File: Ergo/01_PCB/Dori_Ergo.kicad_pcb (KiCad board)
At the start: 2 copper layers, 306.4 x 117.5 mm, 207 parts, among them J1 TYPE-C-31-M12_13, J2 AVR-ISP-6_mod, J3 4PIN, J4 4PIN, J5 TYPE-C-31-M12_13, J6 AVR-ISP-6_mod, K1 KEYSW, K10 KEYSW, K11 KEYSW, K12 KEYSW, K13 KEYSW, K14 KEYSW, K15 KEYSW, K16 KEYSW, K17 KEYSW, K18 KEYSW, K19 KEYSW, K2 KEYSW, K20 KEYSW, K21 KEYSW, K22 KEYSW, K23 KEYSW, K24 KEYSW, K25 KEYSW, K26 KEYSW, K27 KEYSW, K28 KEYSW, K29 KEYSW, K3 KEYSW, K30 KEYSW, K31 KEYSW, K32 KEYSW, K33 KEYSW, K34 KEYSW, K35 KEYSW, K36 KEYSW, K37 KEYSW, K38 KEYSW, K39 KEYSW, K4 KEYSW, K40 KEYSW, K41 KEYSW, K42 KEYSW, K43 KEYSW, K44 KEYSW, K45 KEYSW, K46 KEYSW, K47 KEYSW, K48 KEYSW, K49 KEYSW, K5 KEYSW, K50 KEYSW, K51 KEYSW, K52 KEYSW, K53 KEYSW, K54 KEYSW, K55 KEYSW, K56 KEYSW, K6 KEYSW, K7 KEYSW, K8 KEYSW, K9 KEYSW, SW1 SW_PUSH, SW10 Rotary_Encoder_Switch, SW2 SW_PUSH, SW3 Rotary_Encoder_Switch, SW4 Rotary_Encoder_Switch, SW5 Rotary_Encoder_Switch, SW6 Rotary_Encoder_Switch, SW7 Rotary_Encoder_Switch, SW8 Rotary_Encoder_Switch, SW9 Rotary_Encoder_Switch, U1 ATMEGA32U4, U10 HOLE, U11 HOLE, U12 ATMEGA32U4, U13 HOLE, U14 HOLE, U15 HOLE, U16 HOLE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

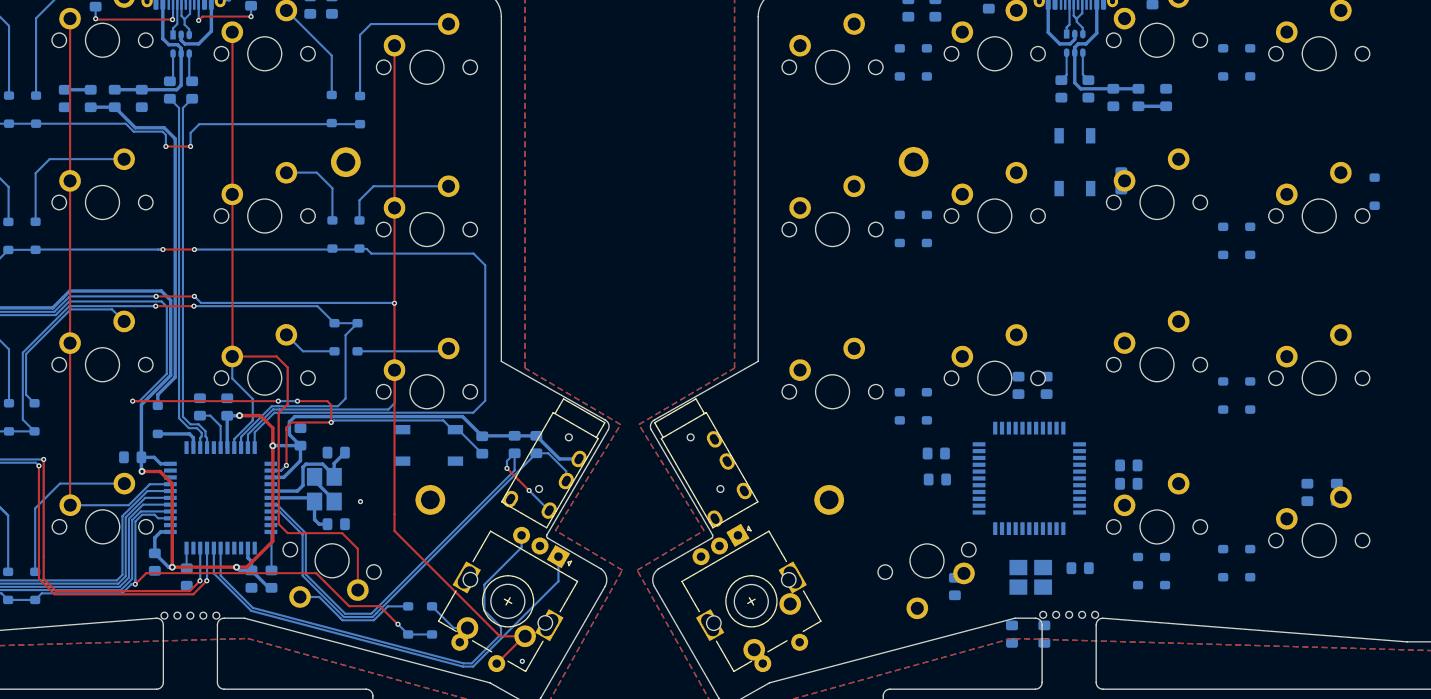
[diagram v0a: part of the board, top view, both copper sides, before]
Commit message: Add ergo layout
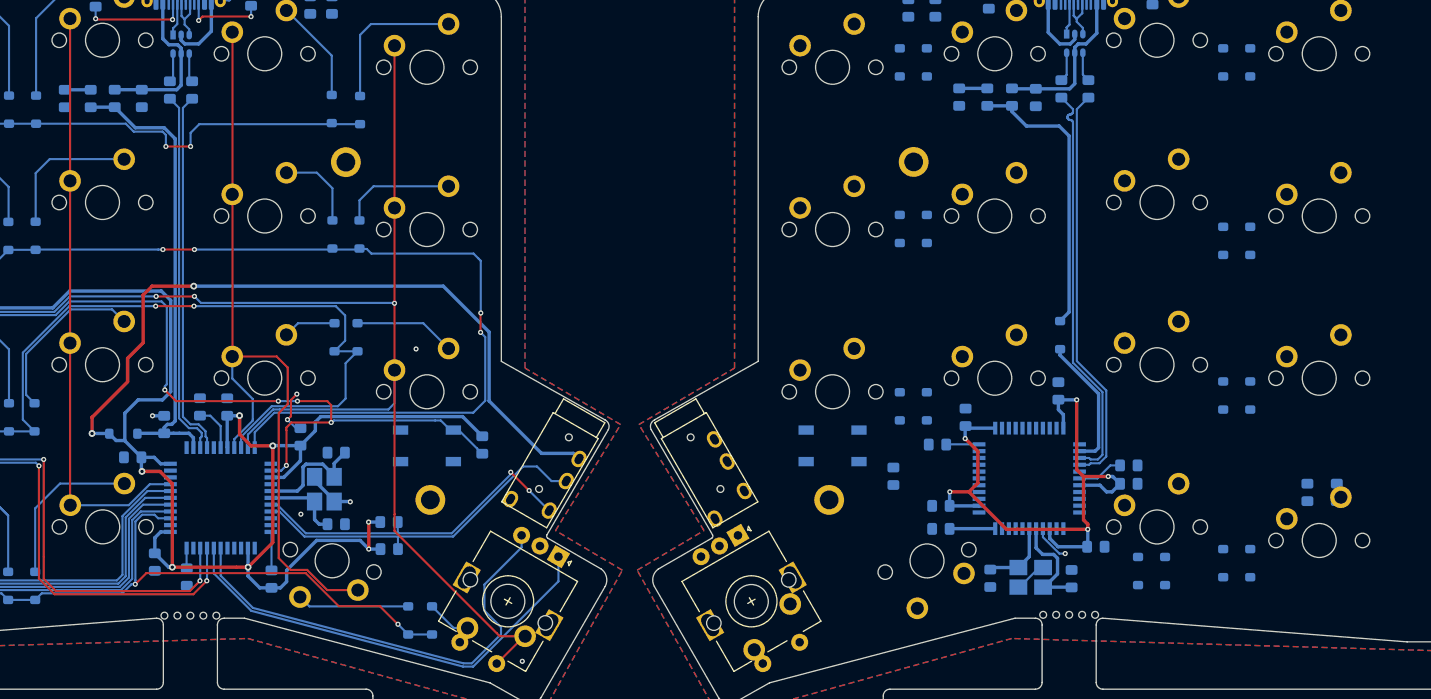
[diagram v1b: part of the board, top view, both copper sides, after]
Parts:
- added LED2: LED, LED_SMD:LED_0805_2012Metric_Pad1.15x1.40mm_HandSolder, B.Cu at (283.9, 54.3)
- C1, C2, C3, C4: value 100nF -> .1uF
- R5, R6: value 4.7K -> 4.7k
- moved RSW2 43.8 mm to (276.2, 98.8)
- moved SW2 43.8 mm to (269.1, 95.2), turned to 180 degrees
- moved D54 40.6 mm to (295.8, 82.2)
- moved R6 21.2 mm to (217.0, 107.4), turned to 0 degrees
- moved R9 21.0 mm to (287.2, 54.3)
- moved C5 20.8 mm to (190.6, 92.8), turned to 90 degrees
- moved R5 17.3 mm to (217.0, 104.2), turned to 0 degrees
- moved F2 14.9 mm to (290.1, 54.3)
- moved CESD2 9.10 mm to (292.9, 54.4)
- moved C9 7.26 mm to (284.7, 91.9)
- moved CX3 7.25 mm to (297.1, 110.8), turned to 90 degrees
- moved CX4 7.04 mm to (287.6, 110.8)
- moved R14 6.97 mm to (281.8, 105.0), turned to 0 degrees
- moved D53 4.36 mm to (185.8, 93.8), turned to 0 degrees
- moved C11 3.13 mm to (281.8, 102.3)
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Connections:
- C5 pad 1: VCC -> UVcca
- D53 pad 1: UVcca -> VCC
- D53 pad 2: +5V -> UVcca
- F1 pad 1: +5V -> UVcca
- R4 pad 2: +5V -> UVcca
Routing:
- net VCC: track 177.6 -> 273.1 mm, vias 5 -> 9
- net VDD: track 0.00 -> 75.2 mm, vias 0 -> 5
- net UVcca: track 5.52 -> 54.8 mm
- net Db-: track 0.00 -> 47.7 mm
- net Db+: track 0.00 -> 47.7 mm
- net +5V: track 43.7 -> 0.00 mm
- net +5VA: track 3.25 -> 33.6 mm
- net UVccb: track 0.00 -> 15.8 mm
- net SCLa: track 54.9 -> 40.4 mm
- net XTAL1b: track 0.00 -> 12.8 mm
- net SDAa: track 52.6 -> 41.5 mm
- net GND: track 12.3 -> 21.0 mm, vias 4 -> 9
- net XTAL2b: track 0.00 -> 8.50 mm
- net GNDA: track 8.45 -> 16.7 mm, vias 0 -> 1
- net ISP_RSTa: track 115.7 -> 109.4 mm
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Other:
- net class Thick: via_dia 1 -> 0.8; via_drill 0.8 -> 0.4

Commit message: Finished left half
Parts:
- moved C4 20.5 mm to (200.8, 111.0), turned to 270 degrees
- moved D53 5.99 mm to (191.4, 91.7), turned to 90 degrees
- moved C5 3.61 mm to (193.6, 90.8)
- moved C6 2.50 mm to (197.2, 91.2)
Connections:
- C5 pad 1: UVcca -> +5V
- D53 pad 2: UVcca -> +5V
- F1 pad 1: UVcca -> +5V
- J2 pad 2: VCC -> +5V
- R4 pad 2: UVcca -> +5V
- U1 pad 2: UVcca -> +5V
- U1 pad 7: VCC -> +5V
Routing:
- net +5V: track 0.00 -> 93.8 mm, vias 0 -> 2
- net VCC: track 273.1 -> 195.5 mm, vias 9 -> 8
- net UVcca: track 54.8 -> 0.00 mm
- net Net-(C6-Pad1): track 5.47 -> 3.24 mm
- net GND: track 21.0 -> 22.9 mm, vias 9 -> 10
- net Da-: track 43.1 -> 42.6 mm
- net Da+: track 43.1 -> 42.6 mm

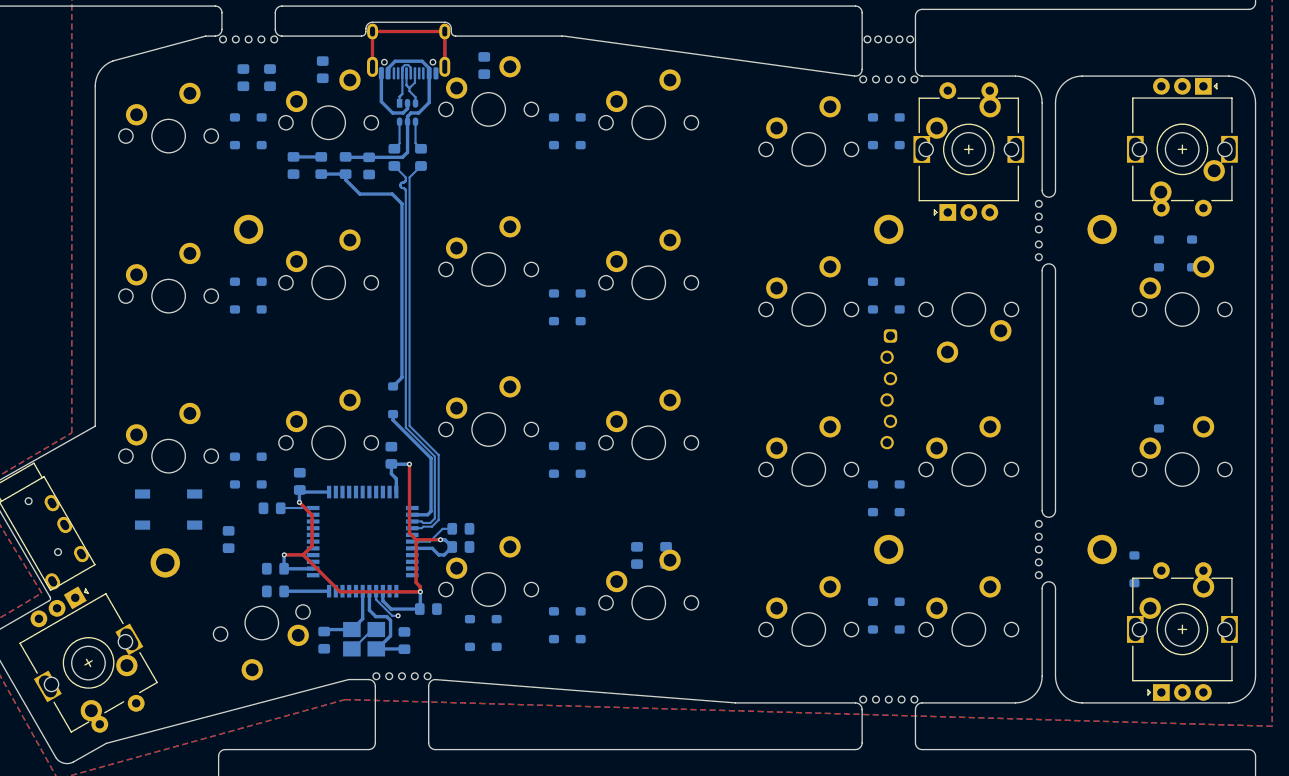
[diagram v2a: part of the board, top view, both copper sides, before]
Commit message: Ergo routing
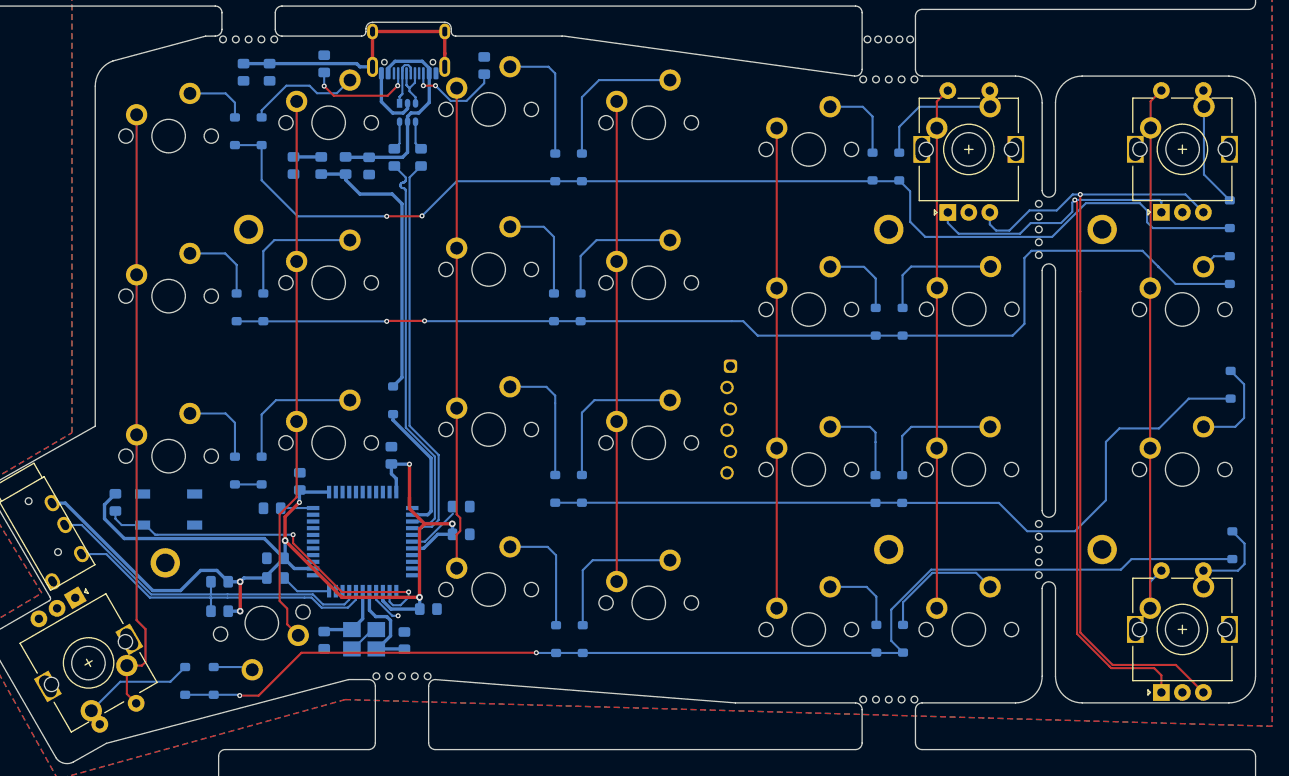
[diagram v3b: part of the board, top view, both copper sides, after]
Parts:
- moved R7 53.6 mm to (275.1, 107.3), turned to 180 degrees
- moved R8 49.8 mm to (275.1, 103.8), turned to 180 degrees
- moved D43 34.4 mm to (271.1, 115.7)
- moved D44 34.2 mm to (274.4, 115.7)
- moved J6 19.4 mm to (335.8, 84.5)
- moved RSW2 14.2 mm to (262.8, 94.4)
- moved D58 12.0 mm to (395.7, 99.5)
- moved D57 9.24 mm to (395.5, 80.4)
- moved D56 8.66 mm to (395.4, 66.8)
- moved D55 6.48 mm to (395.4, 60.1)
- moved D10 4.30 mm to (318.3, 54.5)
- moved D9 4.30 mm to (315.1, 54.5)
- moved D11 4.20 mm to (352.9, 54.4)
- moved D12 4.20 mm to (356.0, 54.4)
- moved D33 3.45 mm to (315.1, 92.8)
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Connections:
- C5 pad 1: +5V -> UVcca
- D53 pad 2: +5V -> UVcca
- F1 pad 1: +5V -> UVcca
- J2 pad 2: +5V -> VCC
- R4 pad 2: +5V -> UVcca
- RSW2 pad 2: +5VA -> VDD
- U1 pad 2: +5V -> UVcca
- U1 pad 7: +5V -> VCC
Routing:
- net row3b: track 0.00 -> 136.4 mm, vias 0 -> 2
- net row0b: track 0.00 -> 134.8 mm, vias 0 -> 2
- net row1b: track 0.00 -> 129.5 mm, vias 0 -> 2
- net Enc3b: track 0.00 -> 99.6 mm, vias 0 -> 1
- net Enc3a: track 0.00 -> 96.8 mm, vias 0 -> 1
- net row2b: track 0.00 -> 95.6 mm
- net col0b: track 0.00 -> 72.9 mm
- net VDD: track 75.2 -> 143.1 mm, vias 5 -> 7
- net col6b: track 0.00 -> 67.2 mm
- net col1b: track 0.00 -> 65.3 mm
- net col5b: track 0.00 -> 62.2 mm
- net col2b: track 0.00 -> 57.5 mm
- net col4b: track 0.00 -> 57.2 mm
- net col3b: track 0.00 -> 57.2 mm
- net ISP_RSTb: track 0.00 -> 44.7 mm, vias 0 -> 2
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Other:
- net class Power added: clearance 0.13, trace_width 0.4, via_dia 0.8, via_drill 0.4
- net class Thick removed

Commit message: Routing ergo
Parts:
- moved C11 0.65 mm to (281.8, 101.7)
- moved R14 0.65 mm to (281.8, 104.0)
- moved C7 0.50 mm to (296.1, 88.8)
- moved D54 0.45 mm to (295.8, 81.8)
- moved R7 0.30 mm to (275.1, 107.0)
- moved R8 0.20 mm to (275.1, 104.0)
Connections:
- U12 pad 1: (no net) -> row0b
- U12 pad 21: (no net) -> row3b
- U12 pad 25: row3b -> col0b
- U12 pad 26: row2b -> (no net)
- U12 pad 27: col0b -> (no net)
- U12 pad 28: col1b -> (no net)
- U12 pad 29: col2b -> (no net)
- U12 pad 36: row0b -> row2b
- U12 pad 37: row1b -> col1b
- U12 pad 42: (no net) -> row1b
- U12 pad 8: col6b -> col2b
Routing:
- net col5b: track 62.2 -> 137.4 mm, vias 0 -> 1
- net col4b: track 57.2 -> 113.2 mm
- net ISP_RSTb: track 44.7 -> 99.9 mm
- net MOSIb: track 0.00 -> 46.9 mm
- net row0b: track 134.8 -> 174.5 mm
- net col0b: track 72.9 -> 107.6 mm
- net VDD: track 143.1 -> 170.0 mm
- net row1b: track 129.5 -> 151.1 mm
- net row2b: track 95.6 -> 74.4 mm
- net col1b: track 65.3 -> 78.0 mm
- net row3b: track 136.4 -> 145.5 mm, vias 2 -> 3
- net col2b: track 57.5 -> 63.5 mm, vias 0 -> 1
- net GNDA: track 16.7 -> 18.1 mm, vias 1 -> 2
- net Net-(C12-Pad1): track 6.22 -> 7.05 mm
- net SDAb: track 40.5 -> 41.1 mm

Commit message: Finished routing Ergo
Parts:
- moved C10 22.4 mm to (281.8, 101.8), turned to 180 degrees
- moved C11 22.0 mm to (302.3, 93.7), turned to 0 degrees
- moved C12 2.72 mm to (303.6, 97.6)
- moved D54 0.30 mm to (295.5, 81.8)
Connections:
- C11 pad 1: VDD -> +5VA
- C5 pad 1: UVcca -> +5V
- D53 pad 2: UVcca -> +5V
- D54 pad 1: UVccb -> VDD
- F1 pad 1: UVcca -> +5V
- J2 pad 2: VCC -> +5V
- J6 pad 2: VDD -> +5VA
- R4 pad 2: UVcca -> +5V
- U1 pad 2: UVcca -> +5V
- U1 pad 7: VCC -> +5V
- U12 pad 12: (no net) -> row3b
- U12 pad 2: UVccb -> +5VA
- U12 pad 20: col3b -> (no net)
- U12 pad 21: row3b -> (no net)
- U12 pad 27: (no net) -> Enc2a
- U12 pad 28: (no net) -> Enc2b
- U12 pad 29: (no net) -> row2b
- U12 pad 30: Enc2b -> (no net)
- U12 pad 31: Enc2a -> (no net)
- U12 pad 36: row2b -> (no net)
- U12 pad 40: (no net) -> col6b
- U12 pad 41: (no net) -> col3b
- U12 pad 7: VDD -> +5VA
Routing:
- net col6b: track 67.2 -> 193.1 mm, vias 0 -> 2
- net Enc3b: track 99.6 -> 211.1 mm, vias 1 -> 4
- net Enc3a: track 96.8 -> 204.0 mm, vias 1 -> 4
- net +5VA: track 33.2 -> 112.3 mm, vias 0 -> 2
- net row2b: track 74.4 -> 149.1 mm, vias 0 -> 4
- net VDD: track 170.0 -> 113.9 mm
- net col3b: track 57.2 -> 107.2 mm, vias 0 -> 3
- net Enc2b: track 0.00 -> 41.7 mm, vias 0 -> 2
- net Enc2a: track 0.00 -> 35.2 mm, vias 0 -> 2
- net col0a: track 125.1 -> 144.1 mm, vias 0 -> 1
- net UVccb: track 16.3 -> 0.00 mm
- net Db-: track 47.7 -> 52.5 mm
- net Db+: track 47.7 -> 52.5 mm
- net row0b: track 174.5 -> 171.4 mm, vias 2 -> 3
- net GNDA: track 18.1 -> 20.4 mm, vias 2 -> 6
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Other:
- board text added: "github.com/dierickdie Dori Ergo Rev 1.0"
- board text removed: "Dori Rev 1.1"
- board text removed: "github.com/dierickdie"

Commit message: Update
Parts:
- moved J6 9.43 mm to (344.5, 81.0), turned to 90 degrees
- moved J2 7.94 mm to (154.8, 76.6)
- moved D15 5.30 mm to (172.2, 75.9)
- moved D16 5.30 mm to (175.4, 75.9)
- moved D17 3.70 mm to (210.4, 74.1)
- moved D18 3.70 mm to (213.5, 74.1)
- moved D25 1.90 mm to (134.1, 93.8)
- moved D26 1.90 mm to (137.3, 93.8)
- moved D27 1.85 mm to (172.4, 93.8)
- moved D28 1.85 mm to (175.4, 93.8)
- moved D21 1.36 mm to (315.2, 69.8)
- moved D22 1.36 mm to (318.3, 69.8)
- moved D23 1.25 mm to (353.2, 71.7)
- moved D24 1.25 mm to (356.4, 71.7)
- moved D33 0.60 mm to (315.1, 93.4)
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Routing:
- net VDD: track 113.9 -> 135.9 mm, vias 7 -> 9
- net +5VA: track 112.3 -> 131.1 mm
- net MOSIb: track 46.9 -> 63.1 mm
- net col5b: track 137.4 -> 146.8 mm
- net ISP_RSTb: track 100.3 -> 109.5 mm
- net col4b: track 113.2 -> 121.3 mm, vias 0 -> 1
- net ISP_RSTa: track 109.9 -> 103.3 mm
- net row2b: track 149.1 -> 155.5 mm
- net Net-(D16-Pad2): track 16.7 -> 22.1 mm
- net row2a: track 201.9 -> 207.2 mm
- net Net-(D15-Pad2): track 10.2 -> 15.5 mm
- net +5V: track 93.8 -> 99.1 mm
- net Net-(D27-Pad2): track 12.5 -> 16.9 mm
- net col5a: track 175.2 -> 170.8 mm
- net Net-(D28-Pad2): track 20.5 -> 24.7 mm
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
